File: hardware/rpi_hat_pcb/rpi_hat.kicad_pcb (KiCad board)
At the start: 2 copper layers, 65 x 56 mm, 5 parts, among them J1 GPIO

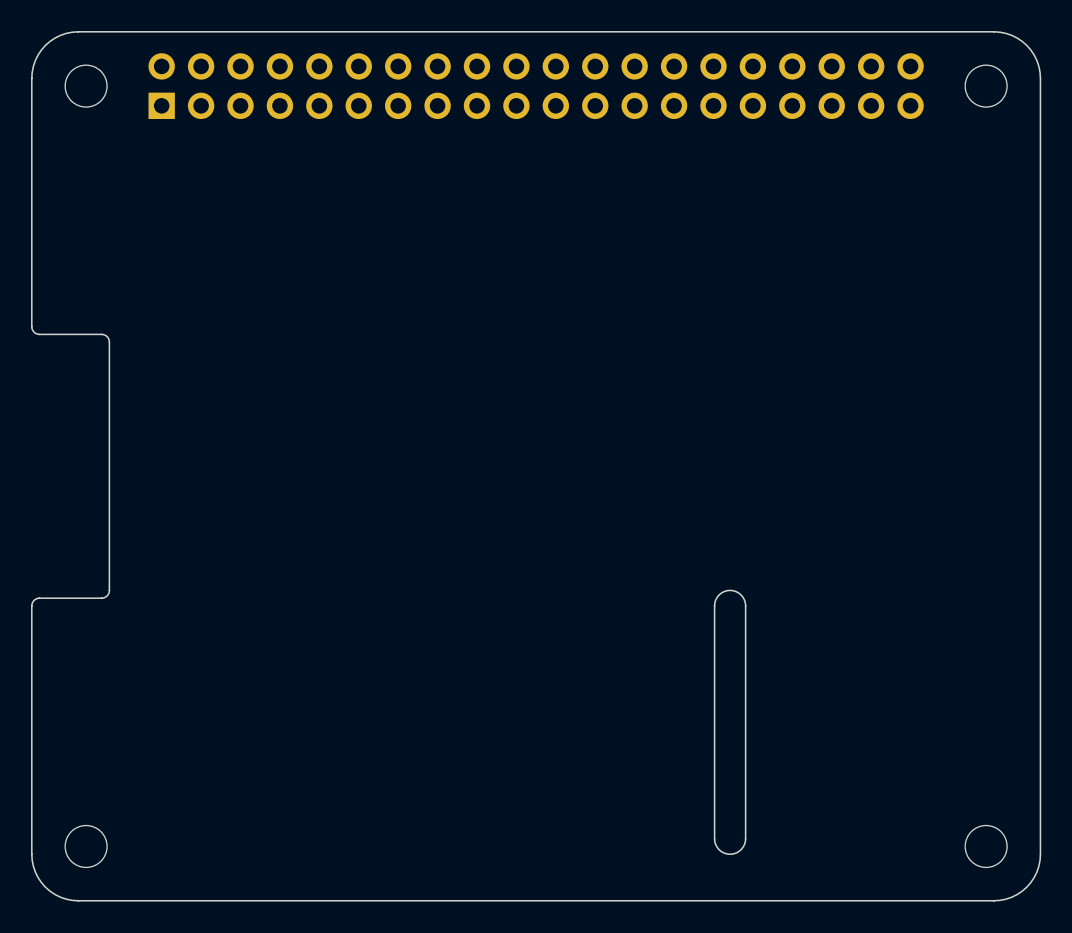
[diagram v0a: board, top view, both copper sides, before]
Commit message: Update the pcb layout and spice simulation
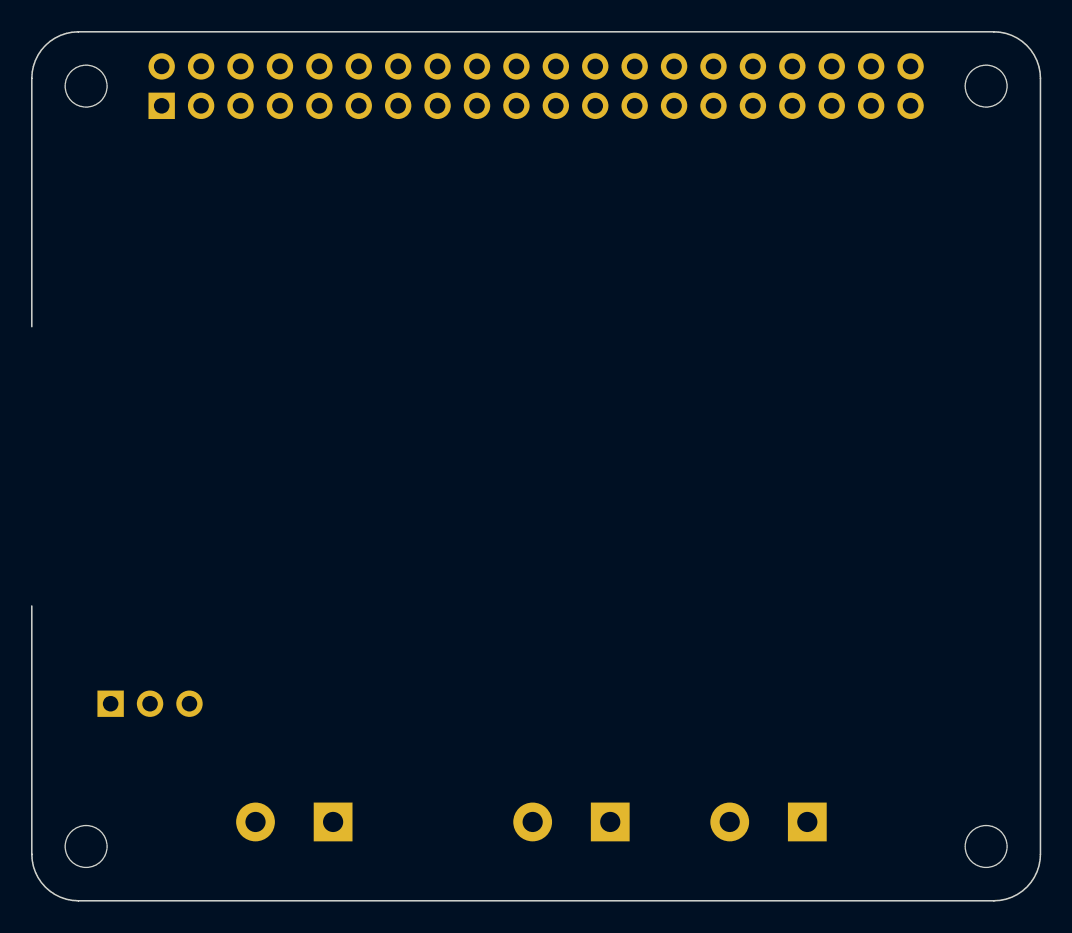
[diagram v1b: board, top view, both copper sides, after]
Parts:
- added J2: OSTTC020162, digikey-footprints:Term_Block_1x2_P5mm, B.Cu at (150.0, 94.9)
- added J3: OSTTC020162, digikey-footprints:Term_Block_1x2_P5mm, B.Cu at (137.3, 94.9)
- added J4: OSTTC020162, digikey-footprints:Term_Block_1x2_P5mm, B.Cu at (119.4, 94.9)
- added M1: Motor_Servo, Connector_PinHeader_2.54mm:PinHeader_1x03_P2.54mm_Vertical, B.Cu at (105.1, 87.3)
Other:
- outline, holes or cut-outs redrawn
- board text added: "Battery - +"
- board text added: "M1 - +"
- board text added: "M2 - +"
- board text added: "Servo (Steering)"
- board text removed: "CAMERA (OPTIONAL)"
- board text removed: "DISPLAY (OPTIONAL)"
- board text removed: "Extend PCB edge 0.5mm if using SMT header"
